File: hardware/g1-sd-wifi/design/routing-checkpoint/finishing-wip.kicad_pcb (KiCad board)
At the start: 6 copper layers, 59 x 115 mm, 351 parts, among them J10 FPGA JTAG pogo pads, J20 5V/GND direct wire pads, J201 microSD push-pull 1.42mm, J202 RP USB service pads, J203 RP SWD/reset/boot pads, J204 C5 direct UART recovery pads, J40 FH12-14S-0.5SH(55), J41 FH12-6S-0.5SH(55), J50 FH12-20S-0.5SH(55), J51 FH12-20S-0.5SH(55), K201 C5 removable compression cont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, K202 C5 removable compression cont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, K203 C5 removable compression cont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, K204 C5 removable compression cont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, K205 C5 removable compression cont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, K206 C5 removable compression cont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, K207 C5 removable compression cont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, K208 C5 removable compression cont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, K209 C5 removable compression cont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, K210 C5 removable compression cont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, K211 C5 removable compression cont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, K212 C5 removable compression cont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, K213 C5 removable compression cont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, K214 C5 removable compression cont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, K215 C5 removable compression cont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, K216 C5 removable compression cont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, Q20 PMV48XP reverse polarity, Q201 C5 recovery pull-down, Q202 C5 recovery pull-down, U10 LCMXO2-2000HC-4TG100C, U20 TPS2116 automatic mux, U201 RP2350B, U202 16MiB boot NOR, U203 8MiB QSPI PSRAM, U204 C5 off-state isolation, U205 C5 off-state isolation, U207 SD4-bit DAT rail isolation, U208 SD CLK/CMD rail isolation, U209 SD enable/power-good NAND, U21 TPS62162 3.3V 1A, U22 TPS62162 3.3V 1A, U23 TPS3808G33DBVR, U24 TPS3808G33DBVR, U25 TPS3808G33DBVR, U26 TPS3808G01DBVR, U27 SN74LVC2G08DCUR, U28 SN74LVC2G08DCUR, U29 SN74LVC2G08DCUR, U30 SN74LVC1G11DBVR, U31 SN74LVC2G04DBVT, U32 SN74LVC1G32DBVR, U33 SN74LVC1G08DBVR, U34 SN74LVC1G08DBVR, U35 SN74LVC16T245, U36 SN74LVC244A host controls, U37 SN74LVC1G17 host RESETn, U38 SN74LVC1G125 qualified ATA_IN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, U39 SN74LVC1G125 qualified ATA_DM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, U40 MX29LV640ETTI-70G x8 / 4 x 2M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, U41 SN74LVC2G125 bank-domain buff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, U42 SN74LVC1G11 write-authorize A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, U43 SN74LVC1G04 write-block inver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, U44 SN74LVC1G332 NOR WE qualifier, U45 TLV803EB29 console-rail NOR r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, U70 SN74LVC1G07 open-drain IORDY, U71 TPS22919 Wi-Fi input switch, U72 SN74LVC1G32DBVR, U73 SN74LVC1G32DBVR, X10 50MHz 3.3V, X201 12MHz

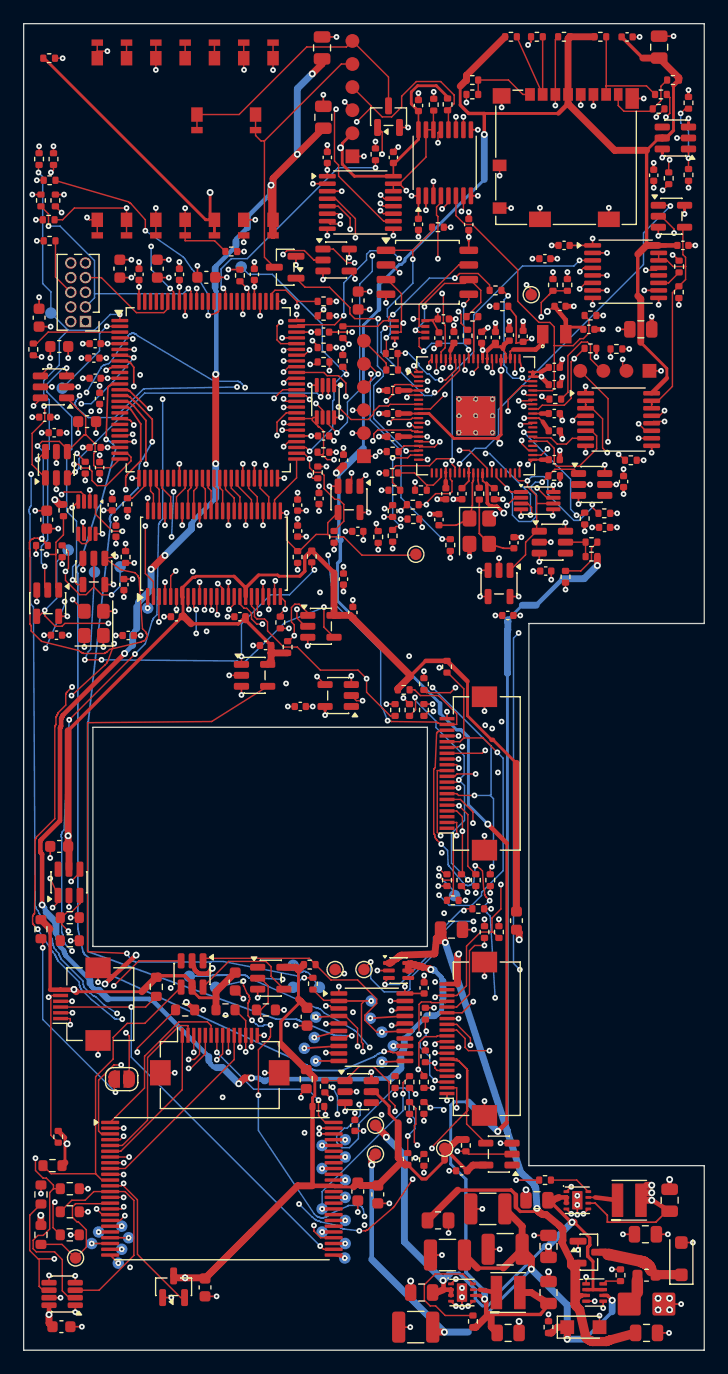
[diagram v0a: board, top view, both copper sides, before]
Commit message: G1 finishing: 12 open, supply check passing (re-finished 42-open session)
check_power_copper.py: a track end within a quarter of its width of
another track's edge taps it, as for pads. A 0.6 mm stub from C211
ends 0.19 mm from the centre of a locked 0.3 mm storage trunk; the
copper overlaps across nearly the stub's full width and KiCad connects
it, but the checker reported C211 unfed.

Co-Authored-By: Claude Opus 5.5 <noreply@anthropic.com>
Claude-Session: https://claude.ai/code/session_01Gp9EYc2r9fMpZ7V8WtfonZ
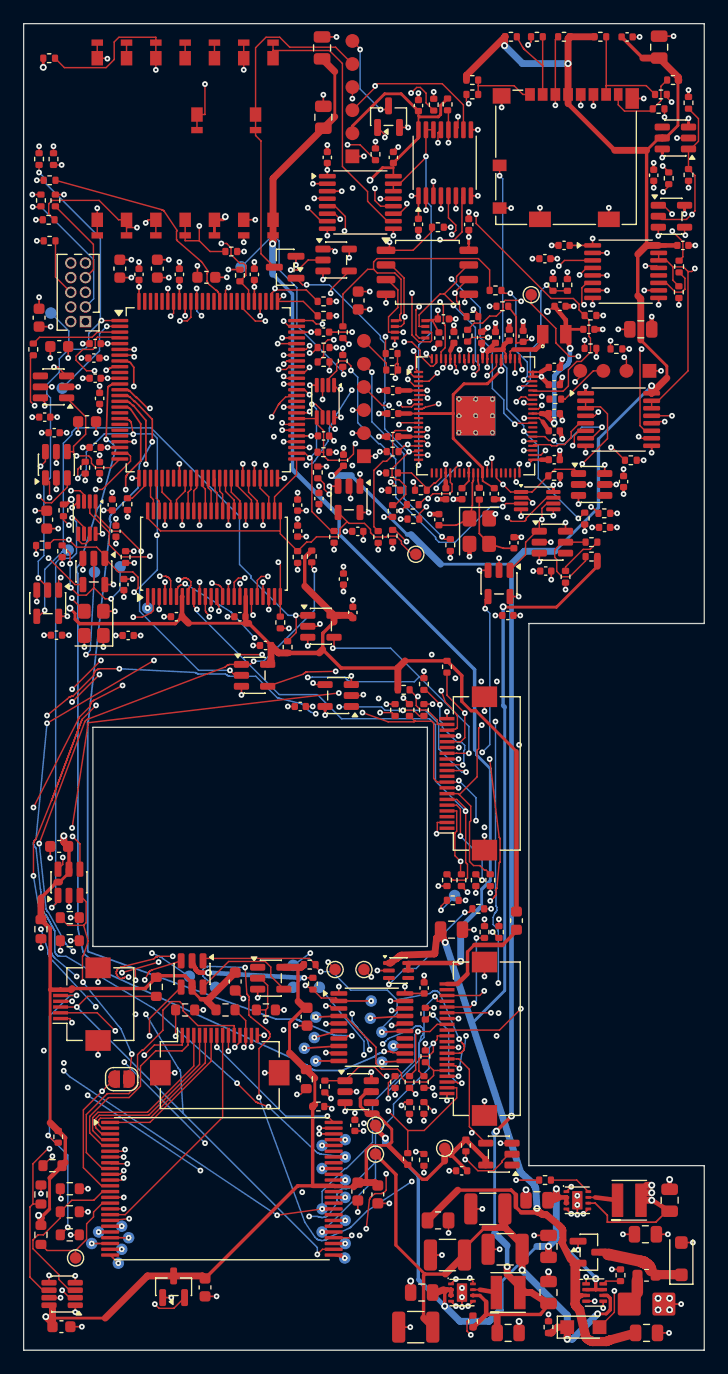
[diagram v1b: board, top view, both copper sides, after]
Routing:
- net IORDY_RELEASE: track 159.4 -> 65.7 mm, vias 13 -> 5
- net ATA_DD8: track 172.6 -> 83.7 mm, vias 9 -> 6
- net ATA_DD15: track 112.8 -> 31.8 mm, vias 5 -> 2
- net ATA_DD14: track 32.6 -> 111.6 mm, vias 4 -> 10
- net INTRQ_OEn: track 40.9 -> 102.5 mm, vias 3 -> 8
- net ATA_CS0n: track 147.5 -> 92.2 mm
- net +5V_C5: track 150.1 -> 95.1 mm, vias 12 -> 2
- net ATA_DD12: track 38.3 -> 87.9 mm
- net ATA_INTRQ: track 57.8 -> 95.4 mm, vias 1 -> 11
- net CONSOLE_3V3: track 296.1 -> 263.9 mm, vias 7 -> 5
- net BUS_SAFE: track 119.3 -> 92.7 mm, vias 7 -> 4
- net ATA_DD9: track 86.0 -> 110.1 mm, vias 4 -> 8
- net +3V3_STORAGE: track 213.5 -> 190.4 mm, vias 5 -> 7
- net ATA_DD6: track 81.5 -> 101.9 mm, vias 5 -> 8
- net ATA_DD0: track 127.0 -> 107.6 mm, vias 5 -> 8
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
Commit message: G1 finishing: 9 open (DRC 0, parity 0, supply check passing)
Boxed-in local connections laid through signal copper on the fine grid,
the cut nets put back by a Freerouting round trip, gaps closed again.

Co-Authored-By: Claude Opus 5.5 <noreply@anthropic.com>
Claude-Session: https://claude.ai/code/session_01Gp9EYc2r9fMpZ7V8WtfonZ
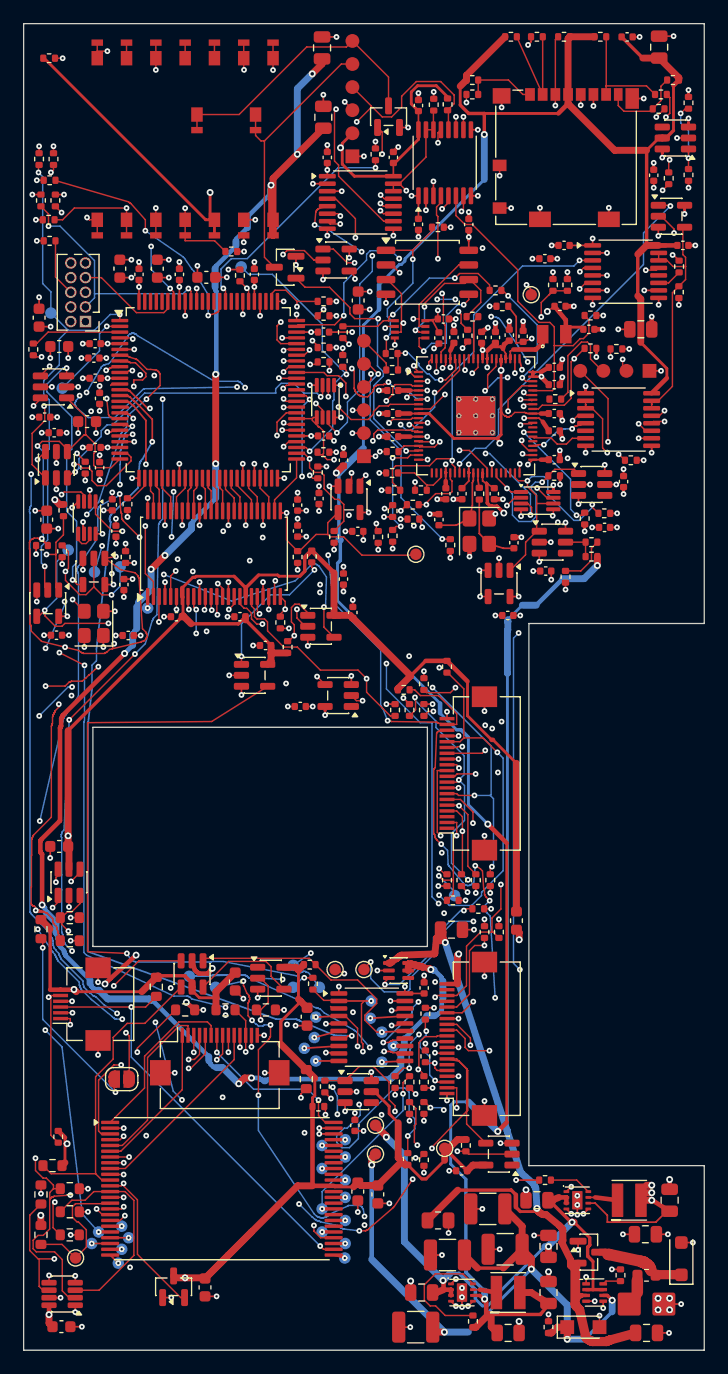
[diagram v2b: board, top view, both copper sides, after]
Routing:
- net IORDY_RELEASE: track 65.7 -> 159.6 mm, vias 5 -> 13
- net ATA_DD8: track 83.7 -> 172.6 mm, vias 6 -> 9
- net ATA_DD15: track 31.8 -> 112.8 mm, vias 2 -> 5
- net BUS_CS0n: track 82.3 -> 2.97 mm, vias 2 -> 1
- net BUS_DA2: track 0.00 -> 77.1 mm, vias 0 -> 8
- net BUS_DMACKn: track 71.9 -> 1.58 mm, vias 2 -> 0
- net ATA_CS0n: track 92.2 -> 147.9 mm, vias 9 -> 10
- net +5V_C5: track 95.1 -> 150.1 mm, vias 2 -> 12
- net ATA_DD12: track 87.9 -> 38.3 mm
- net BIOS_WR_EN: track 10.2 -> 55.5 mm, vias 2 -> 4
- net BIOS_RECOVERYn: track 72.7 -> 112.0 mm, vias 5 -> 10
- net ATA_INTRQ: track 95.4 -> 57.8 mm, vias 11 -> 1
- net CONSOLE_3V3: track 263.9 -> 296.1 mm, vias 5 -> 7
- net BIOS_BANK0: track 92.5 -> 123.2 mm, vias 3 -> 10
- net BUS_SAFE: track 92.7 -> 118.2 mm, vias 4 -> 8
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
